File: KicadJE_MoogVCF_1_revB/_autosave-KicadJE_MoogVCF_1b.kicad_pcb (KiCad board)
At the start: 2 copper layers, 100 x 100 mm, 245 parts, among them J201 CV2, J202 Input2, J203 CV1, J204 Out VCF, J205 Input1, J301 ADSRGate, J302 ADSR, J401 CV, J402 Output, J403 VCA Out, J404 Input, P201 Doepfer_Power_10pin, P301 Doepfer_Power_10pin, P401 Doepfer_Power_10pin, Q201 UMX1N, Q202 SS9014, Q203 SS9014, Q204 SS9014, Q205 SS9014, Q206 SS9014, Q207 SS9014, Q208 UMX1N, Q209 UMX1N, Q210 UMX1N, Q211 SS9014, Q212 SS9015, Q301 SI2302, Q302 MMBT3904, Q303 MMBT3904, Q304 MMBT3904, Q401 UMX1N, Q402 SS9014, SW301 SW_DPDT_x2, SW302 Gate, U201 TL072, U301 TL072, U302 TLC555, U401 TL072, U402 TL074

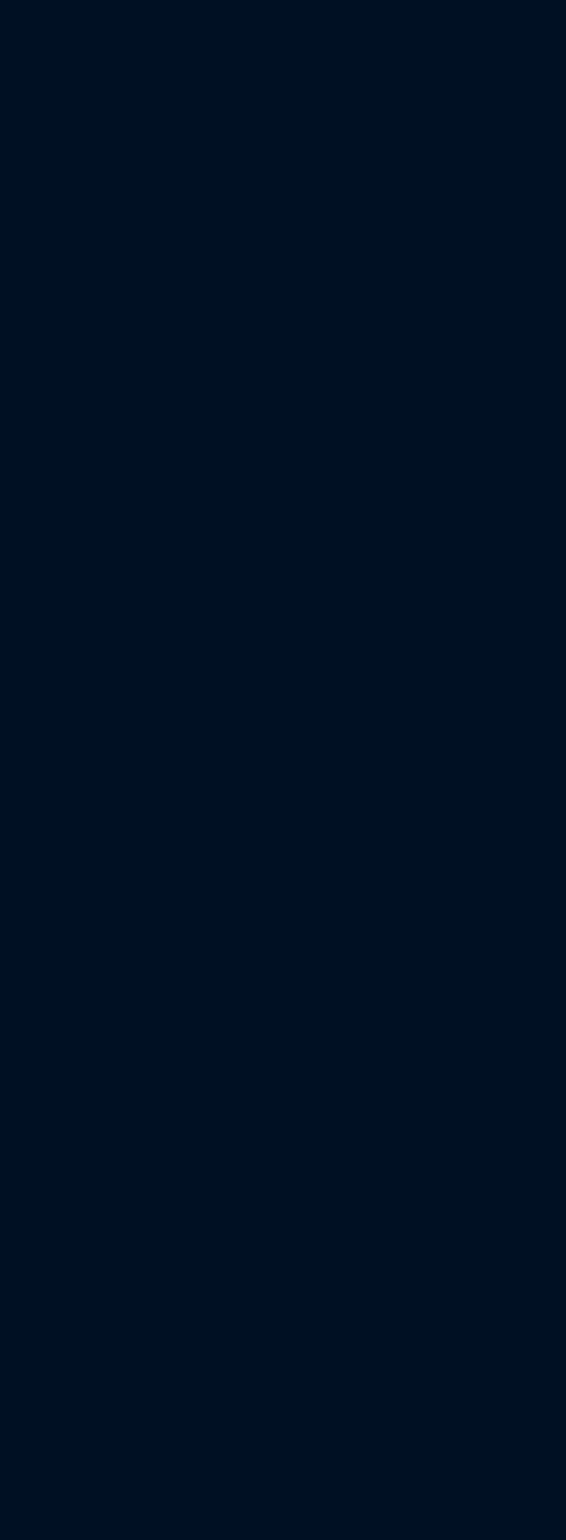
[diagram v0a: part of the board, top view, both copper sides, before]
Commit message: Faceplate for Moog Filter
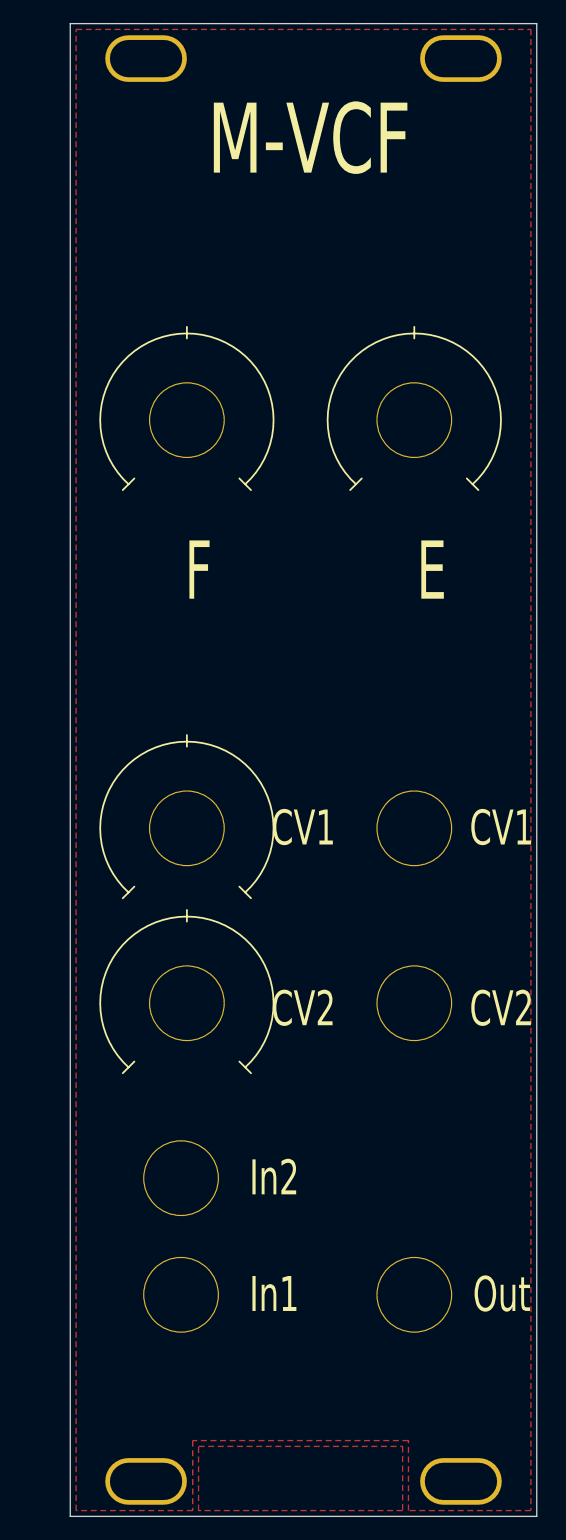
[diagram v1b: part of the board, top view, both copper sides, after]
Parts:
- added G***: LOGO, AJ:Johansen_engineering_soldermask_20mm, F.Cu at (200.0, 161.0)
- added REF**: 6,3mm inner pot, AJ:Pot_6m3_scale1, F.Cu at (209.5, 70.0)
- added REF**: MountingHole_Eurorack3, AJ:MountingHole_Eurorack3, F.Cu at (213.5, 161.0)
- added REF**: MountingHole_Eurorack3, AJ:MountingHole_Eurorack3, F.Cu at (186.5, 161.0)
- added REF**: MountingHole_Eurorack3, AJ:MountingHole_Eurorack3, F.Cu at (213.5, 39.0)
- added REF**: MountingHole_Eurorack3, AJ:MountingHole_Eurorack3, F.Cu at (186.5, 39.0)
- added REF**: 6,3mm inner pot, AJ:Pot_6m3_scale1, F.Cu at (190.0, 70.0)
- added REF**: 6,3mm inner pot, AJ:Pot_6m3_scale1, F.Cu at (190.0, 105.0)
- added REF**: 6,3mm inner pot, AJ:Pot_6m3_scale1, F.Cu at (190.0, 120.0)
- added REF**: 6,3mm inner, AJ:Jack_3m5, F.Cu at (189.5, 135.0)
- added REF**: 6,3mm inner, AJ:Jack_3m5, F.Cu at (209.5, 105.0)
- added REF**: 6,3mm inner, AJ:Jack_3m5, F.Cu at (209.5, 120.0)
- added REF**: 6,3mm inner, AJ:Jack_3m5, F.Cu at (209.5, 145.0)
- added REF**: 6,3mm inner, AJ:Jack_3m5, F.Cu at (189.5, 145.0)
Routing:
- added copper zone on F.Cu, net (none)
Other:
- board size 100 x 100 mm -> 170 x 128 mm
- board text added: "CV1"
- board text added: "CV2"
- board text added: "E"
- board text added: "F"
- board text added: "In1"
- board text added: "In2"
- board text added: "M-VCF"
- board text added: "Out"

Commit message: Update _autosave-KicadJE_MoogVCF_1b.kicad_pcb
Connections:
- REF** pad 1: (no net) -> GND (x10)
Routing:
- removed copper zone on F.Cu, net (none)
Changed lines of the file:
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@@
     (mod_text_size 1 1)
     (mod_text_width 0.15)
-    (pad_size 1.524 1.524)
-    (pad_drill 0.762)
+    (pad_size 6.5 6.5)
+    (pad_drill 6.3)
     (pad_to_mask_clearance 0.051)
     (solder_mask_min_width 0.25)
@@
     )
     (fp_arc (start 0 0) (end 5 5.5) (angle -275.452622) (layer F.SilkS) (width 0.15))
-    (pad 1 thru_hole circle (at 0 0) (size 6.5 6.5) (drill 6.3) (layers *.Cu *.Mask))
+    (pad 1 thru_hole circle (at 0 0) (size 6.5 6.5) (drill 6.3) (layers *.Cu *.Mask)
+      (net 1 GND))
   )
   (module AJ:Pot_6m3_scale1 (layer F.Cu)
@@
     (fp_line (start -4.5 5) (end -5.5 6) (layer F.SilkS) (width 0.15))
     (fp_line (start 0 -8) (end 0 -7) (layer F.SilkS) (width 0.15))
-    (pad 1 thru_hole circle (at 0 0) (size 6.5 6.5) (drill 6.3) (layers *.Cu *.Mask))
+    (pad 1 thru_hole circle (at 0 0) (size 6.5 6.5) (drill 6.3) (layers *.Cu *.Mask)
+      (net 1 GND))
   )
   (module AJ:Jack_3m5 (layer F.Cu)
@@
       (effects (font (size 1 1) (thickness 0.15)))
     )
-    (pad 1 thru_hole circle (at 0 0) (size 6.5 6.5) (drill 6.3) (layers *.Cu *.Mask))
+    (pad 1 thru_hole circle (at 0 0) (size 6.5 6.5) (drill 6.3) (layers *.Cu *.Mask)
+      (net 1 GND))
   )
   (module AJ:Jack_3m5 (layer F.Cu)
@@
     (fp_circle (center 0 0) (end 4.5 0) (layer Cmts.User) (width 0.15))
     (fp_circle (center 0 0) (end 5 0) (layer F.CrtYd) (width 0.05))
-    (pad 1 thru_hole circle (at 0 0) (size 6.5 6.5) (drill 6.3) (layers *.Cu *.Mask))
+    (pad 1 thru_hole circle (at 0 0) (size 6.5 6.5) (drill 6.3) (layers *.Cu *.Mask)
+      (net 1 GND))
   )
   (module AJ:Jack_3m5 (layer F.Cu)
@@
       (effects (font (size 1 1) (thickness 0.15)))
     )
-    (pad 1 thru_hole circle (at 0 0) (size 6.5 6.5) (drill 6.3) (layers *.Cu *.Mask))
+    (pad 1 thru_hole circle (at 0 0) (size 6.5 6.5) (drill 6.3) (layers *.Cu *.Mask)
+      (net 1 GND))
   )
   (module AJ:Jack_3m5 (layer F.Cu)
@@
     (fp_circle (center 0 0) (end 4.5 0) (layer Cmts.User) (width 0.15))
     (fp_circle (center 0 0) (end 5 0) (layer F.CrtYd) (width 0.05))
-    (pad 1 thru_hole circle (at 0 0) (size 6.5 6.5) (drill 6.3) (layers *.Cu *.Mask))
+    (pad 1 thru_hole circle (at 0 0) (size 6.5 6.5) (drill 6.3) (layers *.Cu *.Mask)
+      (net 1 GND))
   )
   (module AJ:MountingHole_Eurorack3 (layer F.Cu)
@@
       (effects (font (size 1 1) (thickness 0.15)))
     )
-    (pad 1 thru_hole oval (at 0 0) (size 7 4) (drill oval 6.2 3.2) (layers *.Cu *.Mask))
+    (pad 1 thru_hole oval (at 0 0) (size 7 4) (drill oval 6.2 3.2) (layers *.Cu *.Mask)
+      (net 1 GND))
   )
   (module AJ:MountingHole_Eurorack3 (layer F.Cu)
@@
       (effects (font (size 1 1) (thickness 0.15)))
     )
-    (pad 1 thru_hole oval (at 0 0) (size 7 4) (drill oval 6.2 3.2) (layers *.Cu *.Mask))
+    (pad 1 thru_hole oval (at 0 0) (size 7 4) (drill oval 6.2 3.2) (layers *.Cu *.Mask)
+      (net 1 GND))
   )
   (module AJ:MountingHole_Eurorack3 (layer F.Cu)
@@
       (effects (font (size 1 1) (thickness 0.15)))
     )
-    (pad 1 thru_hole oval (at 0 0) (size 7 4) (drill oval 6.2 3.2) (layers *.Cu *.Mask))
+    (pad 1 thru_hole oval (at 0 0) (size 7 4) (drill oval 6.2 3.2) (layers *.Cu *.Mask)
+      (net 1 GND))
   )
   (module AJ:MountingHole_Eurorack3 (layer F.Cu)
@@
       (effects (font (size 1 1) (thickness 0.15)))
     )
-    (pad 1 thru_hole oval (at 0 0) (size 7 4) (drill oval 6.2 3.2) (layers *.Cu *.Mask))
+    (pad 1 thru_hole oval (at 0 0) (size 7 4) (drill oval 6.2 3.2) (layers *.Cu *.Mask)
+      (net 1 GND))
   )
   (module Capacitor_SMD:C_1206_3216Metric_Pad1.42x1.75mm_HandSolder (layer F.Cu)
@@
     )
   )
-  (zone (net 0) (net_name "") (layer F.Cu) (hatch edge 0.508)
+  (zone (net 1) (net_name GND) (layer F.Cu) (hatch edge 0.508)
     (connect_pads (clearance 0.508))
     (min_thickness 0.254)
@@
     (polygon
       (pts
-        (xy 208.5 163.5) (xy 191 163.5) (xy 191 158) (xy 208.5 158)
+        (xy 219.5 163.5) (xy 209 163.5) (xy 190.5 163.5) (xy 180.5 163.5) (xy 180.5 36.5)
+        (xy 219.5 36.5)
       )
     )
   )
-  (zone (net 1) (net_name GND) (layer F.Cu) (hatch edge 0.508)
+  (zone (net 1) (net_name GND) (layer B.Cu) (hatch edge 0.508)
     (connect_pads (clearance 0.508))
     (min_thickness 0.254)
@@
     (polygon
       (pts
-        (xy 219.5 163.5) (xy 209 163.5) (xy 209 157.5) (xy 190.5 157.5) (xy 190.5 163.5)
-        (xy 180.5 163.5) (xy 180.5 36.5) (xy 219.5 36.5)
+        (xy 219 164) (xy 181 164) (xy 181 36.5) (xy 219 36.5)
       )
     )
